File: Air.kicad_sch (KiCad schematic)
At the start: 97 parts, among them J1 AIR1, J10 USB_C_Receptacle_USB2.0_14P, J11 Conn_ST_STDC14, J12 CAN, J2 AIR2, J3 AIR3, J4 AIR4, J5 AIR5, J6 AIR6, J7 AIR7, J8 AIR8, J9 24V IN, Q1 2SC2712, Q2 2SC2712, Q3 2SC2712, Q4 2SC2712, Q5 2SC2712, Q6 2SC2712, Q7 2SC2712, Q8 2SC2712, SW1 NRST, U1 TLP293, U10 CH340E, U11 STM32F303K8Tx, U12 MCP2562-E-MF, U2 TLP293, U3 TLP293, U4 TLP293, U5 TLP293, U6 TLP293, U7 TLP293, U8 TLP293, U9 LD1117S33TR

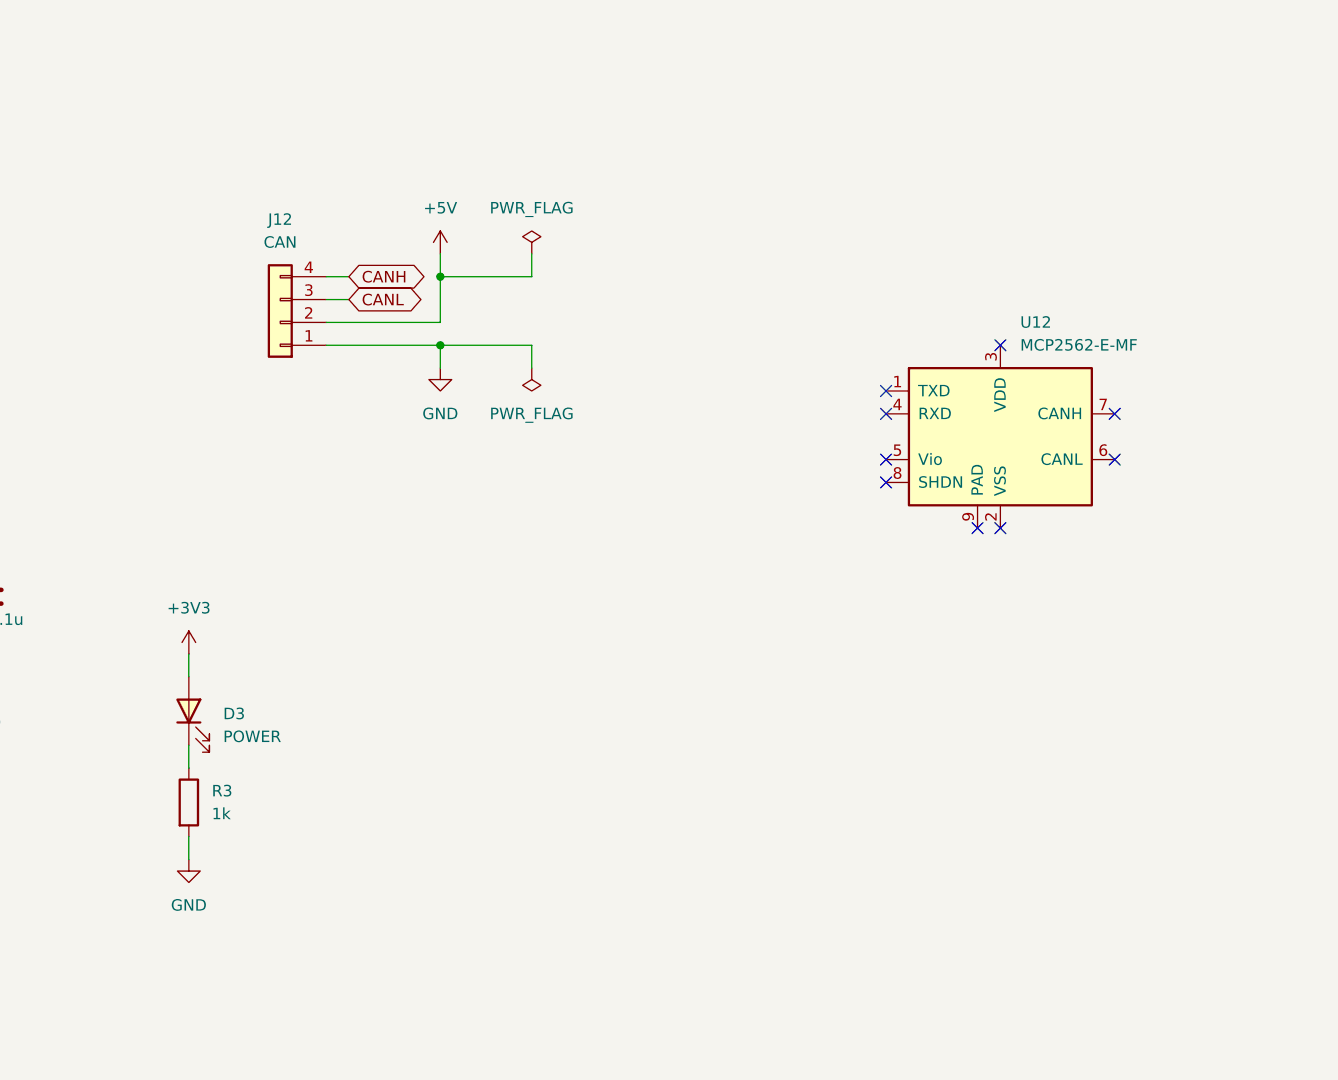
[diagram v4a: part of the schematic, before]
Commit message: Update label size ratio in Air.kicad_pro configuration file
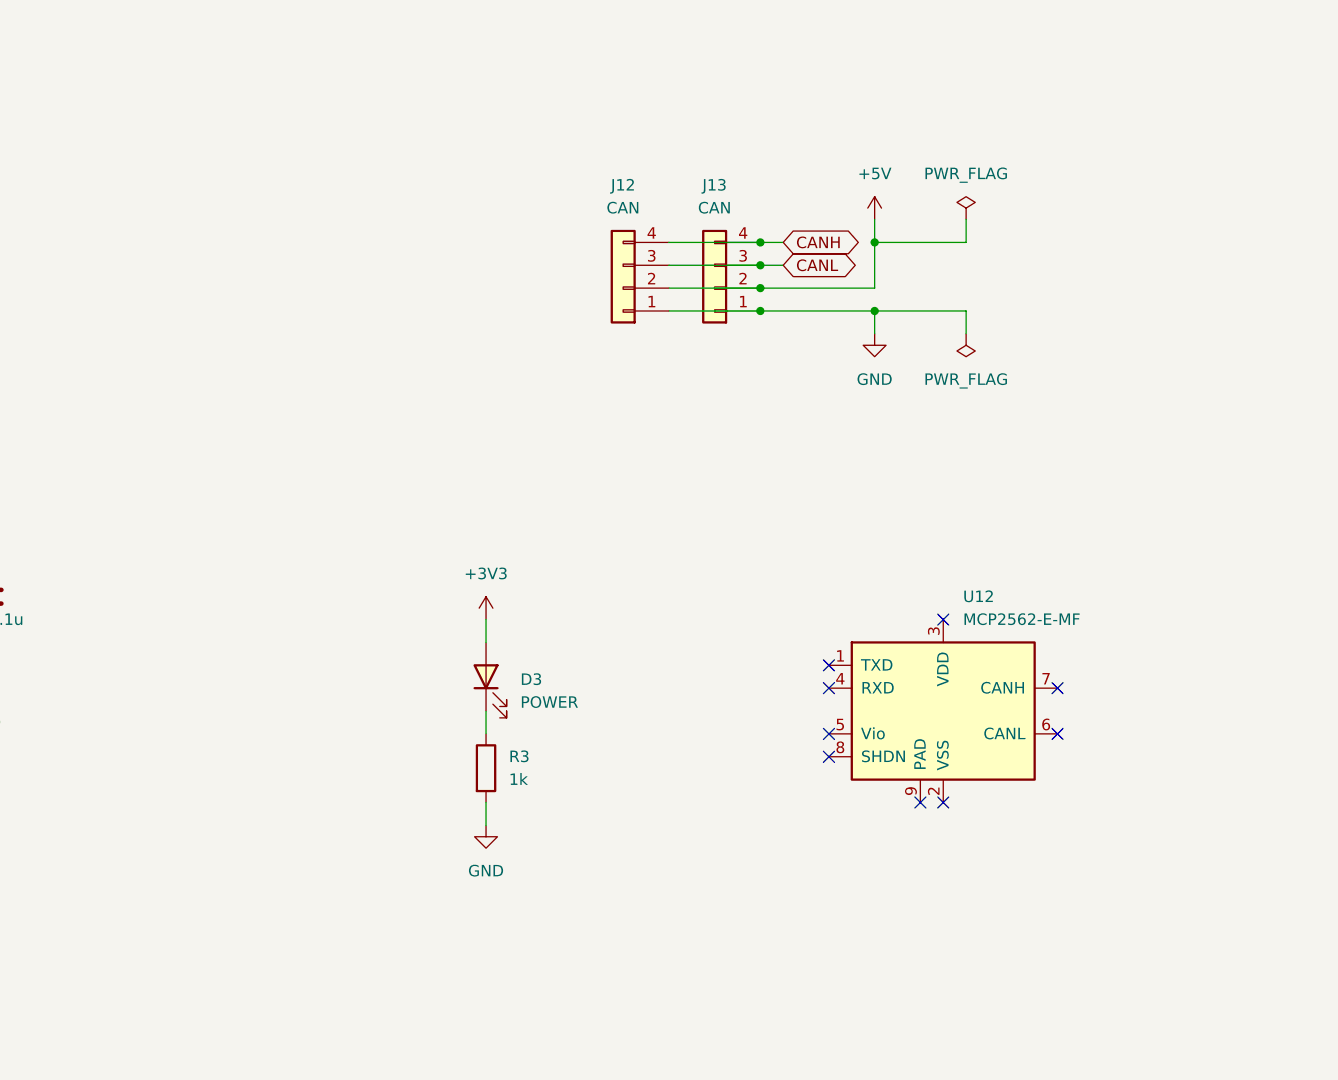
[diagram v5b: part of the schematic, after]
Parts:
- added J12: CAN, symbol Connector_Generic:Conn_01x04
- renumbered J12 to J13
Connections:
- net +5V: now also J12.2 (Pin_2)
- net CANH: now also J12.4 (Pin_4)
- net CANL: now also J12.3 (Pin_3)
- net GND: now also J12.1 (Pin_1)
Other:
- moved on the sheet: D3, J13, R3, U12

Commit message: chore: Update symbol library files for Air and TJA1441
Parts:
- removed D11, D21, D31, D41, D51, D61, D71, D81: SS2040FL, Diode_SMD:D_SOD-123F, symbol Device:D_Schottky_Filled
- removed D12: AIR1, Diode_SMD:D_0603_1608Metric_Pad1.05x0.95mm_HandSolder, symbol Device:LED
- removed D22: AIR2, Diode_SMD:D_0603_1608Metric_Pad1.05x0.95mm_HandSolder, symbol Device:LED
- removed D32: AIR3, Diode_SMD:D_0603_1608Metric_Pad1.05x0.95mm_HandSolder, symbol Device:LED
- removed D42: AIR4, Diode_SMD:D_0603_1608Metric_Pad1.05x0.95mm_HandSolder, symbol Device:LED
- removed D52: AIR5, Diode_SMD:D_0603_1608Metric_Pad1.05x0.95mm_HandSolder, symbol Device:LED
- removed D62: AIR6, Diode_SMD:D_0603_1608Metric_Pad1.05x0.95mm_HandSolder, symbol Device:LED
- removed D72: AIR7, Diode_SMD:D_0603_1608Metric_Pad1.05x0.95mm_HandSolder, symbol Device:LED
- removed D82: AIR8, Diode_SMD:D_0603_1608Metric_Pad1.05x0.95mm_HandSolder, symbol Device:LED
- removed J1: AIR1, Connector_JST:JST_XH_S2B-XH-A_1x02_P2.50mm_Horizontal, symbol Connector_Generic:Conn_01x02
- removed J2: AIR2, Connector_JST:JST_XH_S2B-XH-A_1x02_P2.50mm_Horizontal, symbol Connector_Generic:Conn_01x02
- removed J3: AIR3, Connector_JST:JST_XH_S2B-XH-A_1x02_P2.50mm_Horizontal, symbol Connector_Generic:Conn_01x02
- removed J4: AIR4, Connector_JST:JST_XH_S2B-XH-A_1x02_P2.50mm_Horizontal, symbol Connector_Generic:Conn_01x02
- removed J5: AIR5, Connector_JST:JST_XH_S2B-XH-A_1x02_P2.50mm_Horizontal, symbol Connector_Generic:Conn_01x02
- removed J6: AIR6, Connector_JST:JST_XH_S2B-XH-A_1x02_P2.50mm_Horizontal, symbol Connector_Generic:Conn_01x02
- removed J7: AIR7, Connector_JST:JST_XH_S2B-XH-A_1x02_P2.50mm_Horizontal, symbol Connector_Generic:Conn_01x02
- removed J8: AIR8, Connector_JST:JST_XH_S2B-XH-A_1x02_P2.50mm_Horizontal, symbol Connector_Generic:Conn_01x02
- removed Q1, Q2, Q3, Q4, Q5, Q6, Q7, Q8: 2SC2712, Package_TO_SOT_SMD:SC-59_Handsoldering, symbol Device:Q_NPN_BEC
- removed R11, R12, R13, R14, R21, R22, R23, R24, R31, R32, R33, R34, R41, R42, R43, R44, R51, R52, R53, R54, R61, R62, R63, R64, R71, R72, R73, R74, R81, R82, R83, R84: 10k, Resistor_SMD:R_0603_1608Metric_Pad0.98x0.95mm_HandSolder, symbol Device:R
- removed U1, U2, U3, U4, U5, U6, U7, U8: TLP293, Package_SO:SOIC-4_4.55x2.6mm_P1.27mm, symbol Isolator:TLP293
- removed U12: MCP2562-E-MF, Package_DFN_QFN:DFN-8-1EP_3x3mm_P0.65mm_EP1.55x2.4mm, symbol Interface_CAN_LIN:MCP2562-E-MF
- removed U9: LD1117S33TR, Package_TO_SOT_SMD:SOT-223-3_TabPin2, symbol Regulator_Linear:LD1117S33TR_SOT223
- added C11, C12: 0.1u, symbol Device:C
- added R8: 120, symbol Device:R
- added U12: TJA1441, symbol Air:TJA1441
- added U9: NJM12877, symbol Air:NJM12877
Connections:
- net +3V3: now also C11.1, U12.5 (VIO), U9.5 (VO)
- net +5V: now also C12.1, U12.3 (VCC), U9.1 (VI), U9.3 (CTRL)
- net CAN_RX: now also U12.4 (RXD)
- net CAN_TX: now also U12.1 (TXD)
- net GND: now also C11.2, C12.2, U12.2 (GND), U12.8 (S), U9.2 (GND)
- net CANH: no longer names the net of J12.4 (Pin_4), J13.4 (Pin_4)
- net CANH: now also R8.1, U12.7 (CANH)
- net CANL: no longer names the net of J12.3 (Pin_3), J13.3 (Pin_3)
- net CANL: now also R8.2, U12.6 (CANL)
- net GPIO1 renamed Drive/GPIO1
- net GPIO2 renamed Drive/GPIO2
- net GPIO3 renamed Drive/GPIO3
- net GPIO4 renamed Drive/GPIO4
- net GPIO5 renamed Drive/GPIO5
- net GPIO6 renamed Drive/GPIO6
- net GPIO7 renamed Drive/GPIO7
- net GPIO8 renamed Drive/GPIO8
- no-connect marks 24 -> 18
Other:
- added sheet Drive (Drive.kicad_sch)
- note removed: "NJM12877F33"
- moved on the sheet: C1, C10, C2, C3, C4, C5, C6, C9, D3, J10, J11, J12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

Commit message: feat: Update footprint for JST connectors in Drive and Air schematics
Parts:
- C11, C12: footprint (none) -> Capacitor_SMD:C_0603_1608Metric_Pad1.08x0.95mm_HandSolder
- J10: footprint (none) -> Connector_USB:USB_C_Receptacle_GCT_USB4105-xx-A_16P_TopMnt_Horizontal
- J11: footprint (none) -> Connector_PinHeader_1.27mm:PinHeader_2x07_P1.27mm_Vertical
- J12, J13: footprint (none) -> Connector_JST:JST_XA_S04B-XASK-1_1x04_P2.50mm_Horizontal
- R8: footprint (none) -> Resistor_SMD:R_0603_1608Metric_Pad0.98x0.95mm_HandSolder
- SW1: footprint (none) -> Button_Switch_THT:SW_PUSH_1P1T_6x3.5mm_H4.3_APEM_MJTP1243
- U12: footprint (none) -> Package_SO:SO-8_3.9x4.9mm_P1.27mm
- U9: footprint (none) -> Package_TO_SOT_SMD:SOT-23-5_HandSoldering
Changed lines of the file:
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@@
 			)
 		)
-		(property "Footprint" ""
+		(property "Footprint" "Capacitor_SMD:C_0603_1608Metric_Pad1.08x0.95mm_HandSolder"
 			(at 125.4252 148.59 0)
 			(effects
@@
 			)
 		)
-		(property "Footprint" ""
+		(property "Footprint" "Package_TO_SOT_SMD:SOT-23-5_HandSoldering"
 			(at 158.75 160.02 0)
 			(effects
@@
 			)
 		)
-		(property "Footprint" ""
+		(property "Footprint" "Package_SO:SO-8_3.9x4.9mm_P1.27mm"
 			(at 100.33 160.02 0)
 			(effects
@@
 			)
 		)
-		(property "Footprint" ""
+		(property "Footprint" "Connector_JST:JST_XA_S04B-XASK-1_1x04_P2.50mm_Horizontal"
 			(at 53.34 167.64 0)
 			(effects
@@
 			)
 		)
-		(property "Footprint" ""
+		(property "Footprint" "Connector_JST:JST_XA_S04B-XASK-1_1x04_P2.50mm_Horizontal"
 			(at 63.5 167.64 0)
 			(effects
@@
 			)
 		)
-		(property "Footprint" ""
+		(property "Footprint" "Connector_USB:USB_C_Receptacle_GCT_USB4105-xx-A_16P_TopMnt_Horizontal"
 			(at 205.74 46.99 0)
 			(effects
@@
 			)
 		)
-		(property "Footprint" ""
+		(property "Footprint" "Button_Switch_THT:SW_PUSH_1P1T_6x3.5mm_H4.3_APEM_MJTP1243"
 			(at 90.17 59.69 0)
 			(effects
@@
 			)
 		)
-		(property "Footprint" ""
+		(property "Footprint" "Connector_PinHeader_1.27mm:PinHeader_2x07_P1.27mm_Vertical"
 			(at 48.26 46.99 0)
 			(effects
@@
 			)
 		)
-		(property "Footprint" ""
+		(property "Footprint" "Resistor_SMD:R_0603_1608Metric_Pad0.98x0.95mm_HandSolder"
 			(at 97.282 163.83 90)
 			(effects
@@
 			)
 		)
-		(property "Footprint" ""
+		(property "Footprint" "Capacitor_SMD:C_0603_1608Metric_Pad1.08x0.95mm_HandSolder"
 			(at 110.1852 148.59 0)
 			(effects

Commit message: chore: Update Air.kicad_pro configuration file
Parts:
- added J12: CANR, Connector_PinHeader_2.54mm:PinHeader_1x02_P2.54mm_Vertical, symbol Connector:Conn_01x02_Pin
- renumbered J12 to J13, J13 to J14
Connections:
- net CANL: now reaches J13.3 (Pin_3), J14.3 (Pin_3), R8.2, U12.6 (CANL)
- net CANH: now reaches J13.4 (Pin_4), J14.4 (Pin_4), U12.7 (CANH)
- net CANH: now also J12.1 (Pin_1); no longer R8.1
- new net: J12.2 (Pin_2), R8.1
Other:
- moved on the sheet: J13, J14, R8
